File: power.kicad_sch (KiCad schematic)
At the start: 34 parts, among them J3 CON-USB-DX07S016JA1R1500, J4 CON-S2B-PH-SM4-TB(LF)(SN), U2 nPM1300-QEXX

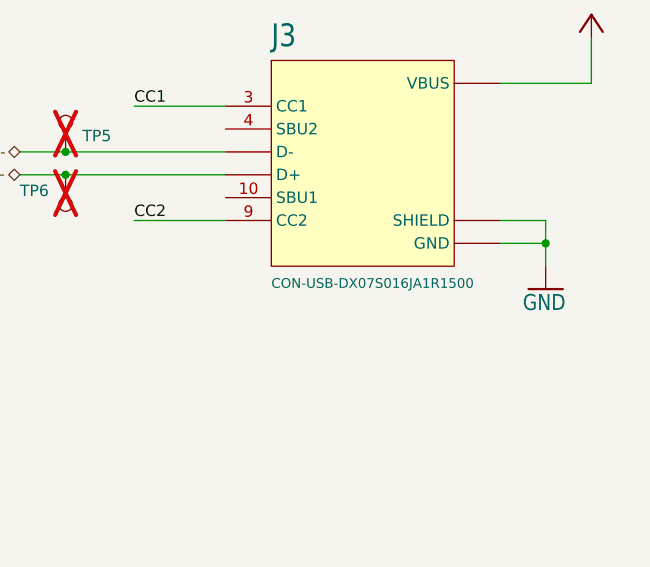
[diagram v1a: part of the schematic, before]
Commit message: Updating parts:
1. Button change
2. USB change
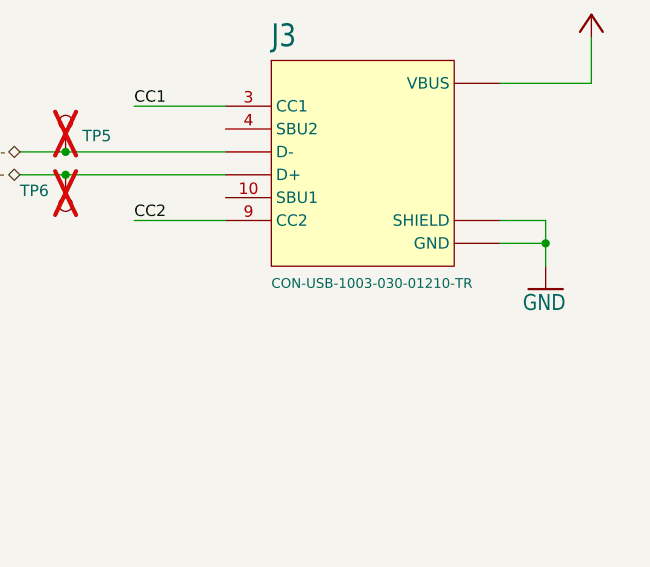
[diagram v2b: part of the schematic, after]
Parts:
- J3: value CON-USB-DX07S016JA1R1500 -> CON-USB-1003-030-01210-TR; footprint Circuit Dojo:JAE_DX07S016JA1R1500 -> Circuit Dojo:CNC_TECH_1003-030-01210-TR
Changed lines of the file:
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@@
 			)
 		)
-		(property "Value" "CON-USB-DX07S016JA1R1500"
+		(property "Value" "CON-USB-1003-030-01210-TR"
 			(at 227.33 144.78 0)
 			(effects
@@
 			)
 		)
-		(property "Footprint" "Circuit Dojo:JAE_DX07S016JA1R1500"
+		(property "Footprint" "Circuit Dojo:CNC_TECH_1003-030-01210-TR"
 			(at 238.76 147.32 0)
 			(effects

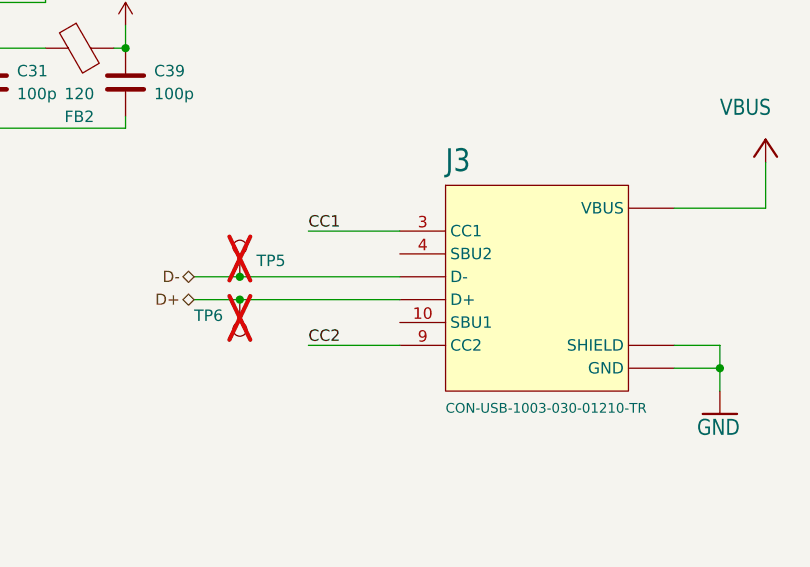
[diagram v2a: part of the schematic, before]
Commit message: Fixing pinout for new USB connector
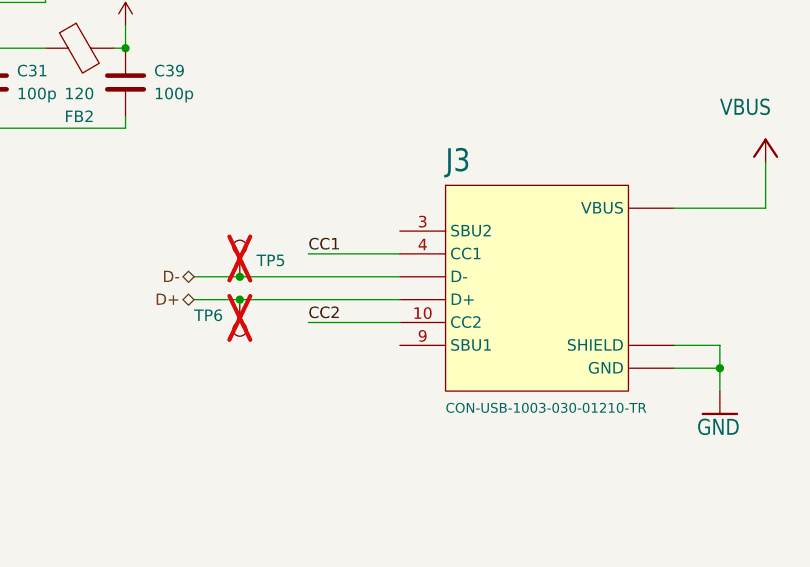
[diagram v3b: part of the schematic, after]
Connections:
- net CC1: now also J3.4 (CC1); no longer J3.3 (CC1)
- net CC2: now also J3.10 (CC2); no longer J3.9 (CC2)
- net D+: now also J3.8 (D+); no longer J3.7 (D+)
- net D-: now also J3.7 (D-); no longer J3.8 (D-)
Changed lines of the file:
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@@
-	(wire
-		(pts
-			(xy 222.25 125.73) (xy 212.09 125.73)
-		)
-		(stroke
-			(width 0.1524)
-			(type solid)
-		)
-	)
 	(wire
 		(pts
@@
 	(wire
 		(pts
+			(xy 212.09 135.89) (xy 222.25 135.89)
+		)
+		(stroke
+			(width 0.1524)
+			(type solid)
+		)
+	)
+	(wire
+		(pts
 			(xy 252.73 123.19) (xy 262.89 123.19)
 		)
@@
 	(wire
 		(pts
-			(xy 212.09 138.43) (xy 222.25 138.43)
-		)
-		(stroke
-			(width 0.1524)
-			(type solid)
-		)
-	)
-	(wire
-		(pts
 			(xy 58.42 93.98) (xy 48.26 93.98)
 		)
@@
 			(width 0)
 			(type default)
+		)
+	)
+	(wire
+		(pts
+			(xy 222.25 128.27) (xy 212.09 128.27)
+		)
+		(stroke
+			(width 0.1524)
+			(type solid)
 		)
 	)
@@
 	)
 	(label "CC2"
-		(at 48.26 93.98 0)
+		(at 212.09 135.89 0)
 		(effects
 			(font
@@
 	)
 	(label "CC2"
-		(at 212.09 138.43 0)
+		(at 48.26 93.98 0)
 		(effects
 			(font
@@
 	)
 	(label "CC1"
-		(at 212.09 125.73 0)
+		(at 212.09 128.27 0)
 		(effects
 			(font

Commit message: Adding variant control
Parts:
- C24, C31, C39, FB2, J3, L2: Var (none) -> Variant Standard(+!) Cptel(-!)
- R4: Circuit Dojo PN.Var (none) -> Standard(RES-255K-1%-0402) Cptel(RES-0R-0402); Var (none) -> Variant Standard(255k) Cptel(0R)
- TP5, TP6: now left out of the parts list
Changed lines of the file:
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@@
 			)
 		)
+		(property "Var" "Variant Standard(255k) Cptel(0R)"
+			(at 48.26 144.78 0)
+			(effects
+				(font
+					(size 1.27 1.27)
+				)
+				(hide yes)
+			)
+		)
+		(property "Circuit Dojo PN.Var" "Standard(RES-255K-1%-0402) Cptel(RES-0R-0402)"
+			(at 48.26 144.78 0)
+			(effects
+				(font
+					(size 1.27 1.27)
+				)
+				(hide yes)
+			)
+		)
 		(pin "1"
 		)
@@
 			)
 		)
+		(property "Var" "Variant Standard(+!) Cptel(-!)"
+			(at 237.49 130.81 0)
+			(effects
+				(font
+					(size 1.27 1.27)
+				)
+				(hide yes)
+			)
+		)
 		(pin "1"
 		)
@@
 			)
 		)
+		(property "Var" "Variant Standard(+!) Cptel(-!)"
+			(at 186.69 105.41 90)
+			(effects
+				(font
+					(size 1.27 1.27)
+				)
+				(hide yes)
+			)
+		)
 		(pin "2"
 		)
@@
 		(unit 1)
 		(exclude_from_sim no)
-		(in_bom yes)
+		(in_bom no)
 		(on_board yes)
 		(dnp yes)
@@
 		(unit 1)
 		(exclude_from_sim no)
-		(in_bom yes)
+		(in_bom no)
 		(on_board yes)
 		(dnp yes)
@@
 			)
 		)
+		(property "Var" "Variant Standard(+!) Cptel(-!)"
+			(at 176.53 109.22 0)
+			(effects
+				(font
+					(size 1.27 1.27)
+				)
+				(hide yes)
+			)
+		)
 		(pin "1"
 		)
@@
 			)
 		)
+		(property "Var" "Variant Standard(+!) Cptel(-!)"
+			(at 191.77 109.22 0)
+			(effects
+				(font
+					(size 1.27 1.27)
+				)
+				(hide yes)
+			)
+		)
 		(pin "1"
 		)
@@
 			)
 		)
+		(property "Var" "Variant Standard(+!) Cptel(-!)"
+			(at 157.48 109.22 90)
+			(effects
+				(font
+					(size 1.27 1.27)
+				)
+				(hide yes)
+			)
+		)
 		(pin "1"
 		)
@@
 			(at 166.37 109.22 0)
 			(effects
+				(font
+					(size 1.27 1.27)
+				)
+				(hide yes)
+			)
+		)
+		(property "Var" "Variant Standard(+!) Cptel(-!)"
+			(at 166.37 109.22 0)
+			(effects
